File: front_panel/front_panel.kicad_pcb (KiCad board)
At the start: 2 copper layers, 82.8 x 28.8 mm, 7 parts

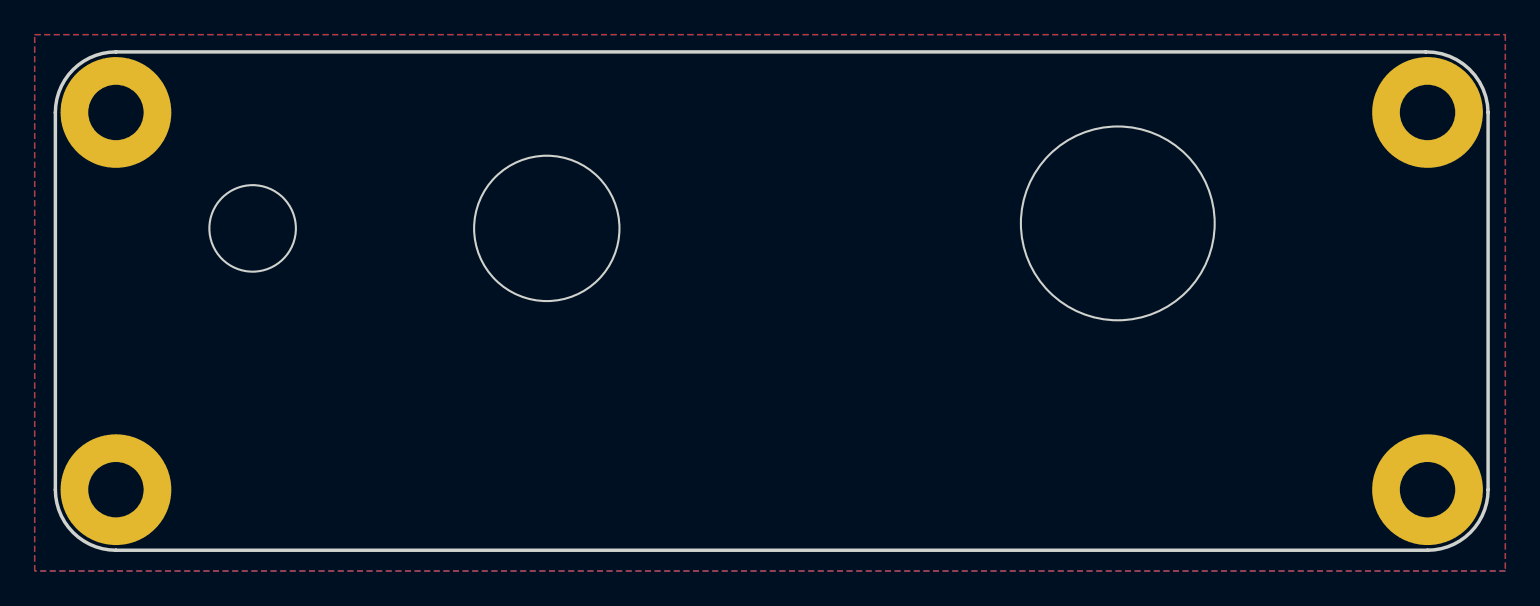
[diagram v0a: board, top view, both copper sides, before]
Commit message: add front panel
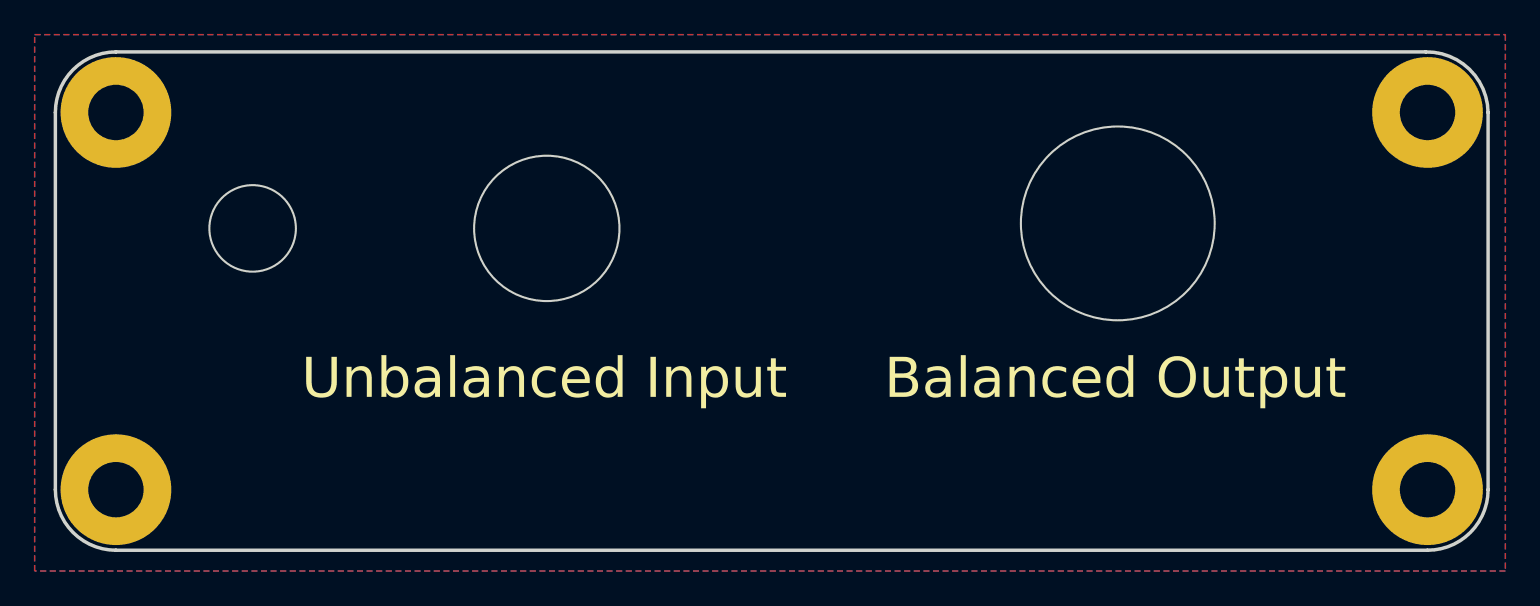
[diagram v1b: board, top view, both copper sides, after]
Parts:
- added svg2mod: G***, unbal2bal_labels:input_label, F.Cu at (162.6, 99.1)
- added svg2mod: G***, unbal2bal_labels:output_label, F.Cu at (195.6, 99.1)
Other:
- board text removed: "TODO: Power label Unbalanced input label Balanced output label unbalanced-to-balanced converter label"

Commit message: minor change from plotting gerbers
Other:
- board text added: "unbal2bal front_panel r0 github.com/gkeeth/unbal2bal 2022-06-17"
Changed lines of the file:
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@@
       (outputformat 1)
       (mirror false)
-      (drillshape 1)
+      (drillshape 0)
       (scaleselection 1)
-      (outputdirectory "")
+      (outputdirectory "../fab/front_panel/")
     )
   )
@@
     (effects (font (size 1 1) (thickness 0.15)) (justify mirror))
   )
+  (gr_text "unbal2bal front_panel r0\ngithub.com/gkeeth/unbal2bal\n2022-06-17" (at 190 103) (layer "B.SilkS")
+    (effects (font (size 1 1) (thickness 0.15)) (justify left mirror))
+  )
   (zone (net 1) (net_name "GND") (layers F&B.Cu) (hatch edge 0.508)

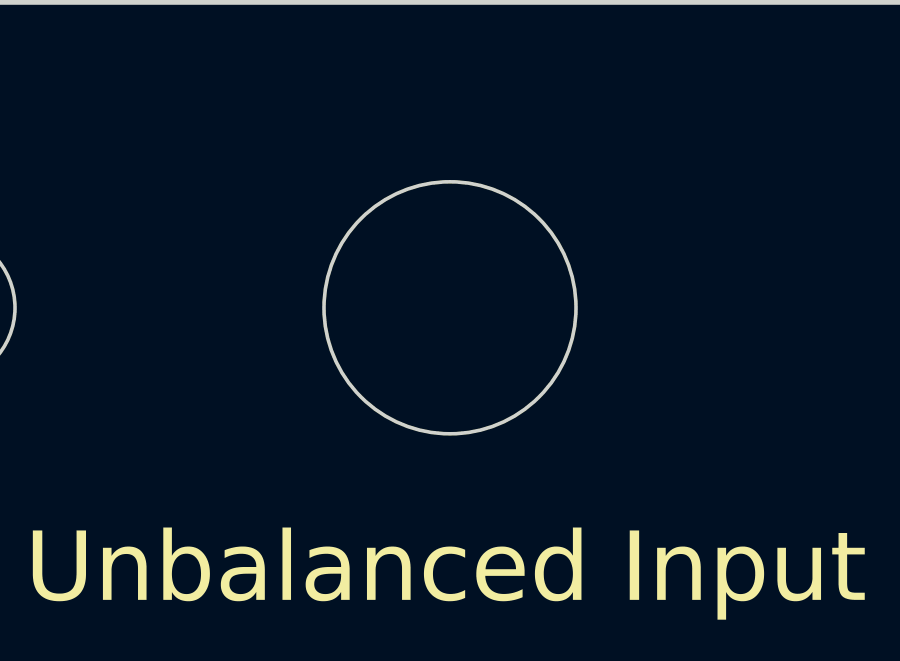
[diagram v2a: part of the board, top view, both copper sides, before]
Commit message: fix vertical position of RCA jack cutout
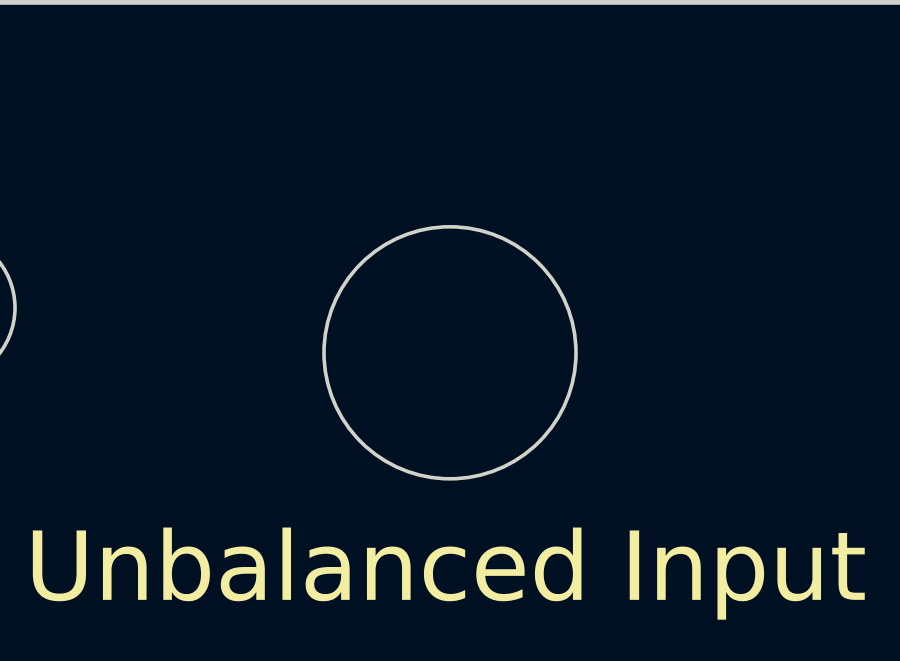
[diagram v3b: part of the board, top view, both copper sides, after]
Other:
- board text added: "unbal2bal front_panel r1 github.com/gkeeth/unbal2bal 2022-07-04"
- board text removed: "unbal2bal front_panel r0 github.com/gkeeth/unbal2bal 2022-06-17"
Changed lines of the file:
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@@
       (effects (font (size 1 1) (thickness 0.15)))
     )
-    (fp_circle (center 0 -8) (end 4.2 -8) (layer "Edge.Cuts") (width 0.12) (fill none))
+    (fp_circle (center 0 -6.5) (end 4.2 -6.5) (layer "Edge.Cuts") (width 0.12) (fill none))
   )
   (footprint "MountingHole:MountingHole_3.2mm_M3_Pad" locked (layer "F.Cu")
@@
     (effects (font (size 1 1) (thickness 0.15)) (justify mirror))
   )
-  (gr_text "unbal2bal front_panel r0\ngithub.com/gkeeth/unbal2bal\n2022-06-17" (at 190 103) (layer "B.SilkS")
+  (gr_text "unbal2bal front_panel r1\ngithub.com/gkeeth/unbal2bal\n2022-07-04" (at 190 103) (layer "B.SilkS")
     (effects (font (size 1 1) (thickness 0.15)) (justify left mirror))
   )

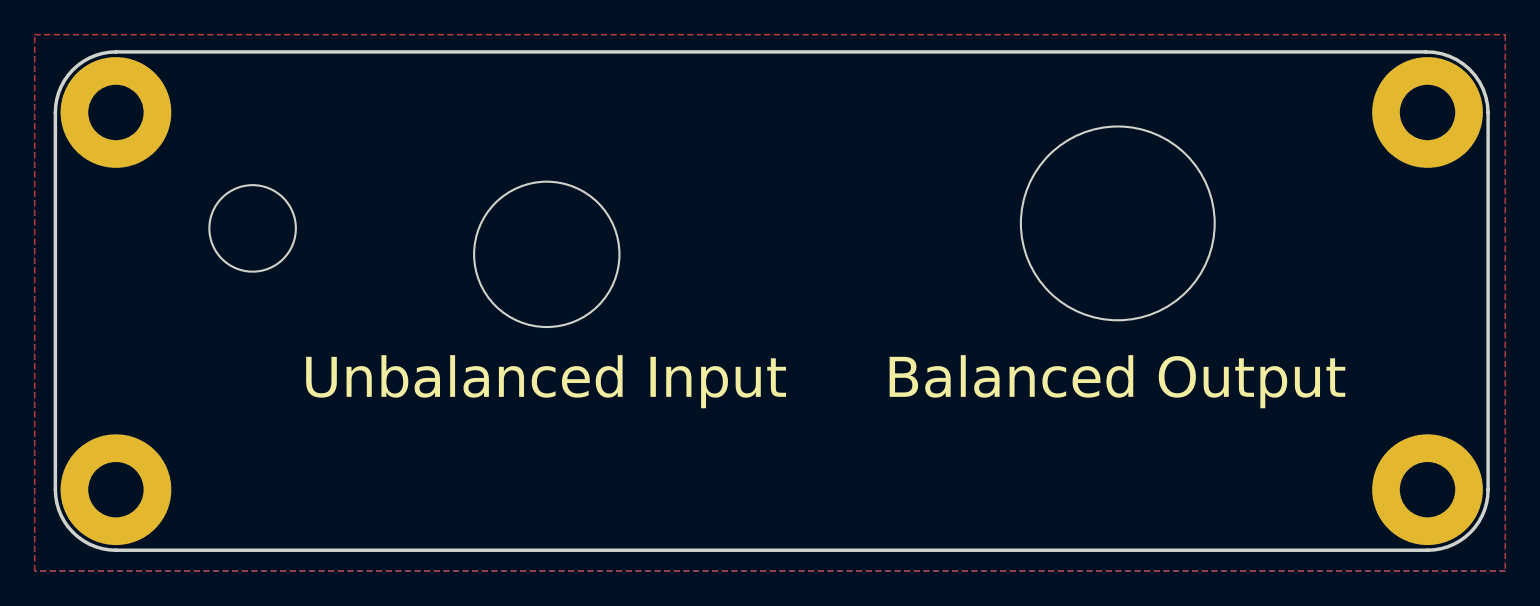
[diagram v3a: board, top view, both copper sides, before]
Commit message: update front panel cutout for 1/4in jack
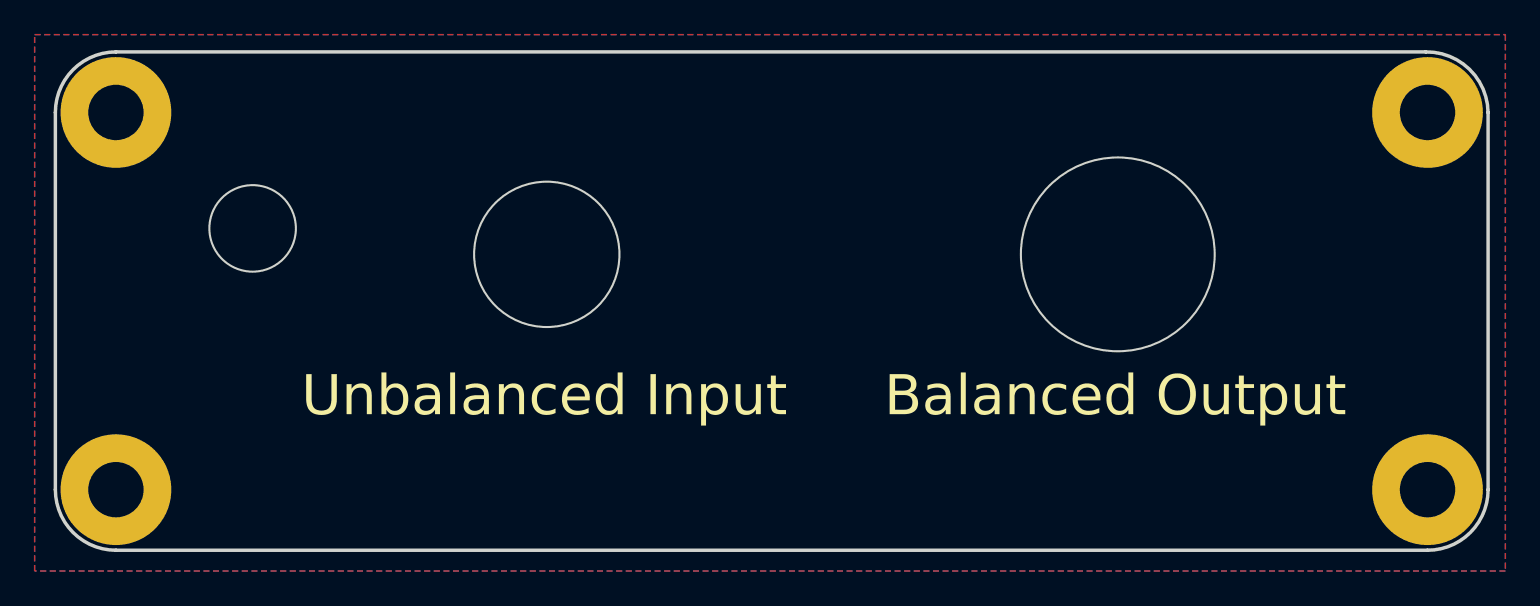
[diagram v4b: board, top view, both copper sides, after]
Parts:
- REF**: value Panel_Jack_6.35mm_Neutrik_NMJ6HFD2 -> Panel_Jack_6.35mm_Neutrik_NRJ3HF-1; footprint Panel_Cutouts:Panel_Jack_6.35mm_Neutrik_NMJ6HFD2 -> Panel_Cutouts:Panel_Jack_6.35mm_Neutrik_NRJ3HF-1
- moved svg2mod 1.00 mm to (162.6, 100.1)
- moved svg2mod 1.00 mm to (195.6, 100.1)
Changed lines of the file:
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@@
   (net 0 "")
   (net 1 "GND")
-  (footprint "Panel_Cutouts:Panel_Jack_6.35mm_Neutrik_NMJ6HFD2" locked (layer "F.Cu")
+  (footprint "Panel_Cutouts:Panel_Jack_6.35mm_Neutrik_NRJ3HF-1" locked (layer "F.Cu")
     (at 195.6 98.2)
     (fp_text reference "REF**" (at 0 -0.5 unlocked) (layer "F.SilkS") hide
       (effects (font (size 1 1) (thickness 0.15)))
     )
-    (fp_text value "Panel_Jack_6.35mm_Neutrik_NMJ6HFD2" (at 0 1 unlocked) (layer "F.Fab")
+    (fp_text value "Panel_Jack_6.35mm_Neutrik_NRJ3HF-1" (at 0 1 unlocked) (layer "F.Fab")
       (effects (font (size 1 1) (thickness 0.15)))
     )
@@
       (effects (font (size 1 1) (thickness 0.15)))
     )
-    (fp_circle (center 0 -8.29) (end 5.6 -8.29) (layer "Edge.Cuts") (width 0.12) (fill none))
+    (fp_circle (center 0 -6.5) (end 5.6 -6.5) (layer "Edge.Cuts") (width 0.12) (fill none))
   )
   (footprint "MountingHole:MountingHole_3.2mm_M3_Pad" locked (layer "F.Cu")
@@
   )
   (footprint "unbal2bal_labels:input_label" (layer "F.Cu")
-    (at 162.56 99.06)
+    (at 162.56 100.06)
     (descr "Converted using: svg2mod -i input_label.svg -o input_label.kicad_mod -p 0.1 --center")
     (tags "svg2mod")
@@
   )
   (footprint "unbal2bal_labels:output_label" (layer "F.Cu")
-    (at 195.58 99.06)
+    (at 195.58 100.06)
     (descr "Converted using: svg2mod -i output_label.svg -o output_label.kicad_mod -p 0.1 --center")
     (tags "svg2mod")

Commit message: update front panel date on silk
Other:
- board text added: "unbal2bal front_panel r1 github.com/gkeeth/unbal2bal 2022-08-28"
- board text removed: "unbal2bal front_panel r1 github.com/gkeeth/unbal2bal 2022-07-04"
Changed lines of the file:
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@@
   )
   (paper "A4")
+  (title_block
+    (title "unbal2bal front panel")
+    (date "2022-08-28")
+    (rev "1")
+    (company "G. Keeth")
+  )
   (layers
     (0 "F.Cu" signal)
@@
     (effects (font (size 1 1) (thickness 0.15)) (justify mirror))
   )
-  (gr_text "unbal2bal front_panel r1\ngithub.com/gkeeth/unbal2bal\n2022-07-04" (at 190 103) (layer "B.SilkS")
+  (gr_text "unbal2bal front_panel r1\ngithub.com/gkeeth/unbal2bal\n2022-08-28" (at 190 103) (layer "B.SilkS")
     (effects (font (size 1 1) (thickness 0.15)) (justify left mirror))
   )

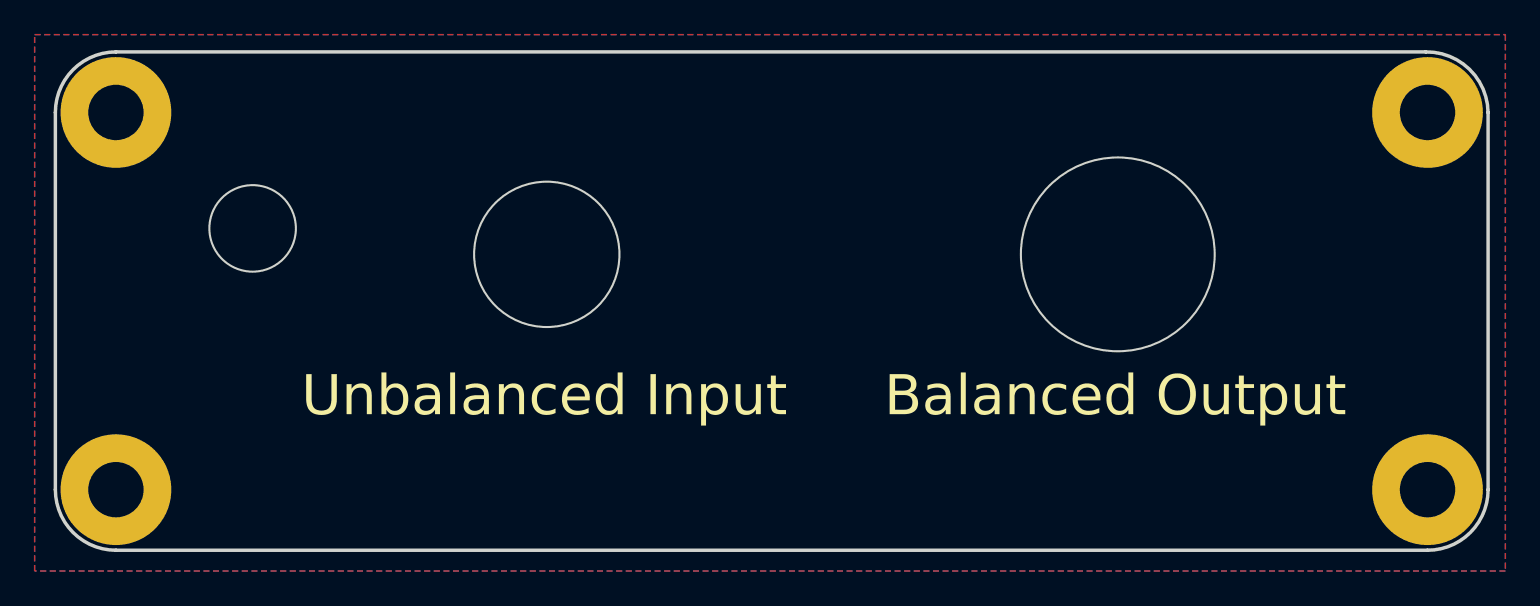
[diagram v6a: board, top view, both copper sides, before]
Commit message: add logo to front panel (r3)
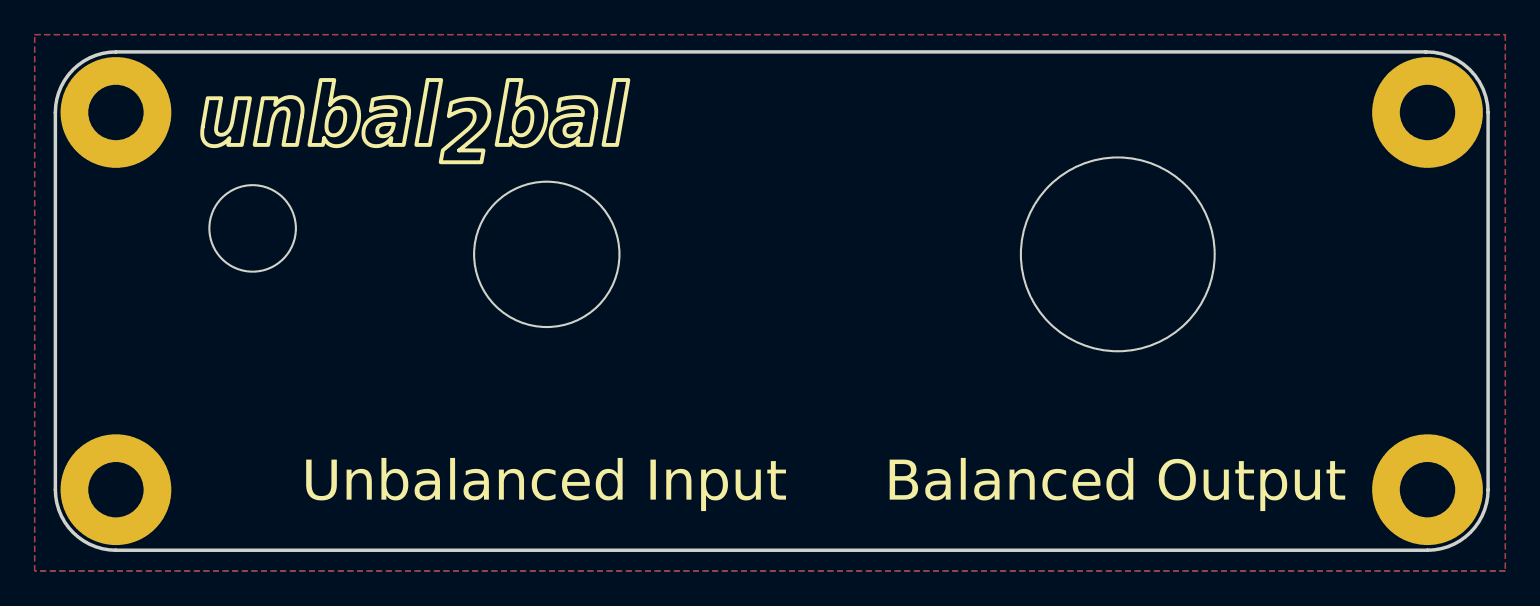
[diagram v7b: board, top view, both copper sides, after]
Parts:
- added svg2mod: G***, unbal2bal_labels:unbal2bal, F.Cu at (155.0, 84.0)
- moved svg2mod 4.94 mm to (162.6, 105.0)
- moved svg2mod 4.94 mm to (195.6, 105.0)
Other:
- board text added: "unbal2bal front_panel r${rev} github.com/gkeeth/unbal2bal ${date}"
- board text removed: "unbal2bal front_panel r1 github.com/gkeeth/unbal2bal 2022-08-28"
